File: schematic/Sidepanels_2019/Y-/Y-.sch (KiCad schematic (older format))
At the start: 53 parts, among them J1 Conn_01x04, J2 Conn_01x02

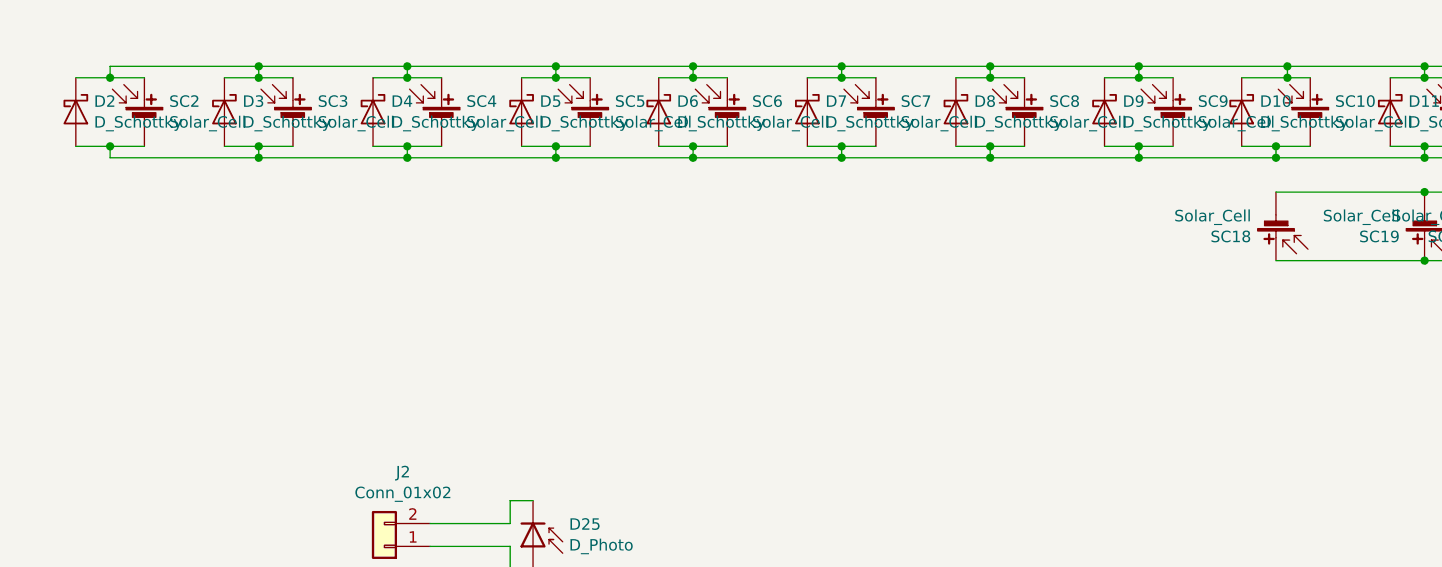
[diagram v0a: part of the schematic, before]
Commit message: Flipped and/or added TrisolX cells
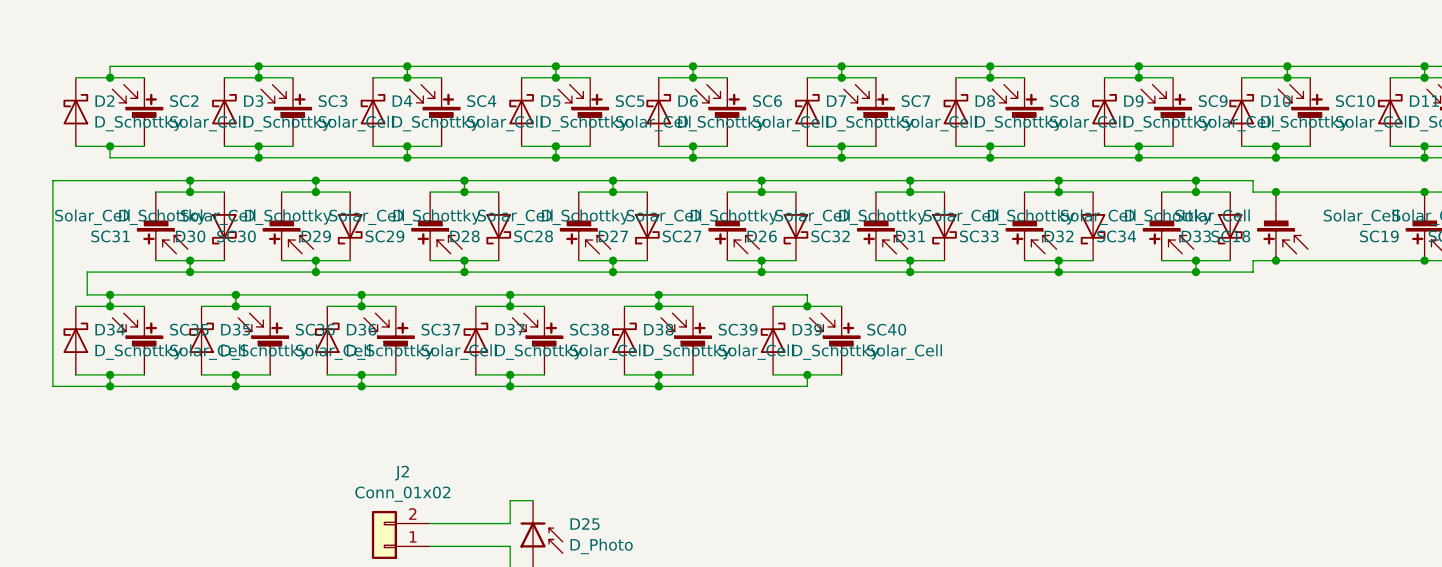
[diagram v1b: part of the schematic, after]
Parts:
- added D26, D27, D28, D29, D30, D31, D32, D33, D34, D35, D36, D37, D38, D39: D_Schottky, CySat footprints:Toshiba_CUS08F30, symbol Device:D_Schottky
- added SC27, SC28, SC29, SC30, SC31, SC32, SC33, SC34, SC35, SC36, SC37, SC38, SC39, SC40: Solar_Cell, CySat footprints:TriSelectSolarPanel_Left_Handed, symbol Device:Solar_Cell
- SC10, SC11, SC12, SC13, SC14, SC15, SC16, SC17, SC2, SC20, SC21, SC22, SC23, SC24, SC25, SC26, SC3, SC4, SC5, SC6, SC7, SC8, SC9: footprint CySat footprints:TriSelectSolarPanel -> CySat footprints:TriSelectSolarPanel_Left_Handed
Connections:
- net VCC: now also D26.1 (K), D27.1 (K), D28.1 (K), D29.1 (K), D30.1 (K), D31.1 (K), D32.1 (K), D33.1 (K), D34.1 (K), D35.1 (K), D36.1 (K), D37.1 (K), D38.1 (K), D39.1 (K), SC27.1 (+), SC28.1 (+), SC29.1 (+), SC30.1 (+), SC31.1 (+), SC32.1 (+), SC33.1 (+), SC34.1 (+), SC35.1 (+), SC36.1 (+), SC37.1 (+), SC38.1 (+), SC39.1 (+), SC40.1 (+)
- net VSS: now also D26.2 (A), D27.2 (A), D28.2 (A), D29.2 (A), D30.2 (A), D31.2 (A), D32.2 (A), D33.2 (A), D34.2 (A), D35.2 (A), D36.2 (A), D37.2 (A), D38.2 (A), D39.2 (A), SC27.2 (-), SC28.2 (-), SC29.2 (-), SC30.2 (-), SC31.2 (-), SC32.2 (-), SC33.2 (-), SC34.2 (-), SC35.2 (-), SC36.2 (-), SC37.2 (-), SC38.2 (-), SC39.2 (-), SC40.2 (-)

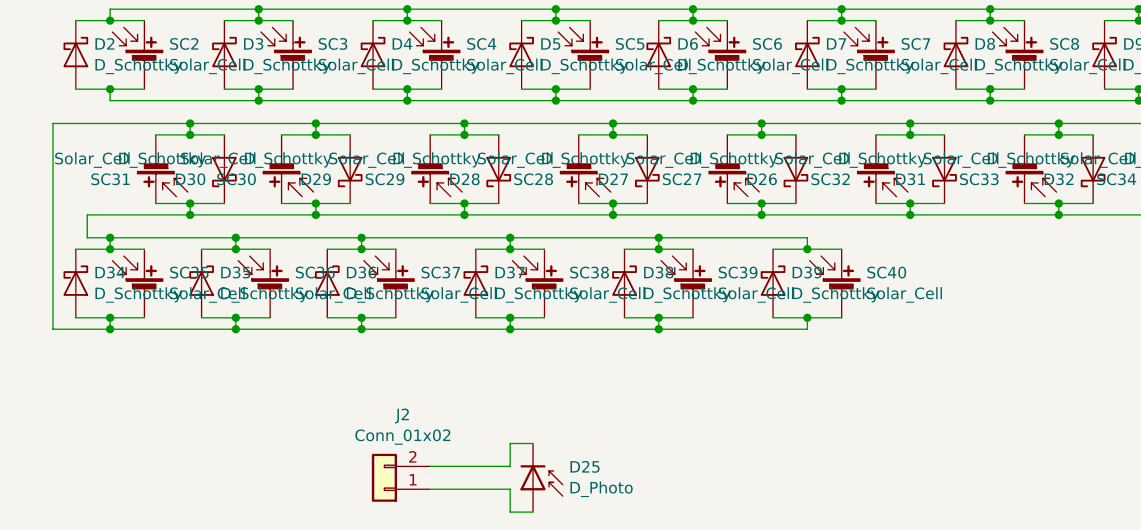
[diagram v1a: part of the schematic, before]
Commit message: Fixed TrisolX Cells
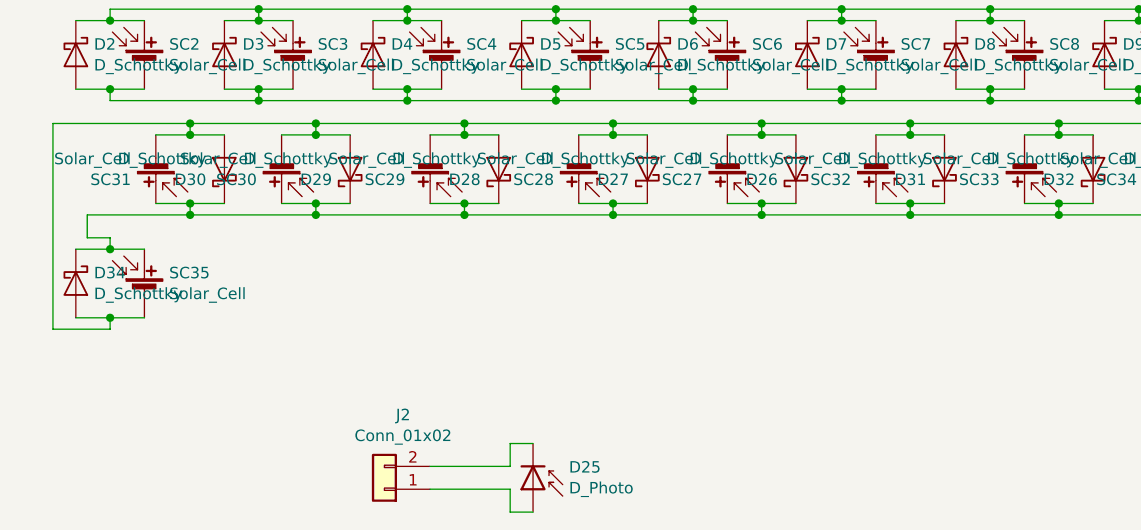
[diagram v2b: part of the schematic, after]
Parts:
- removed D35, D36, D37, D38, D39: D_Schottky, CySat footprints:Toshiba_CUS08F30, symbol Device:D_Schottky
- removed SC36, SC37, SC38, SC39, SC40: Solar_Cell, CySat footprints:TriSelectSolarPanel_Left_Handed, symbol Device:Solar_Cell
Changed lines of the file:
@@
 	5750 3700 5500 3700
 Connection ~ 5500 3700
-Wire Wire Line
-	1300 3850 1450 3850
-Wire Wire Line
-	1300 3850 1300 3800
-Wire Wire Line
-	1300 4150 1150 4150
-Wire Wire Line
-	1300 4150 1300 4200
-Connection ~ 1300 4150
-Wire Wire Line
-	1450 4150 1300 4150
-Connection ~ 1300 3850
-Wire Wire Line
-	1150 3850 1300 3850
-$Comp
-L Device:D_Schottky D35
-U 1 1 5D938735
-P 1150 4000
-F 0 "D35" V 1104 4079 50  0000 L CNN
-F 1 "D_Schottky" V 1195 4079 50  0000 L CNN
-F 2 "CySat footprints:Toshiba_CUS08F30" H 1150 4000 50  0001 C CNN
-F 3 "~" H 1150 4000 50  0001 C CNN
-	1    1150 4000
-	0    1    1    0
-$EndComp
-$Comp
-L Device:Solar_Cell SC36
-U 1 1 5D938703
-P 1450 4050
-F 0 "SC36" H 1558 4146 50  0000 L CNN
-F 1 "Solar_Cell" H 1558 4055 50  0000 L CNN
-F 2 "CySat footprints:TriSelectSolarPanel_Left_Handed" V 1450 4110 50  0001 C CNN
-F 3 "~" V 1450 4110 50  0001 C CNN
-	1    1450 4050
-	1    0    0    -1
-$EndComp
 Connection ~ 1100 3300
 Connection ~ 1100 3700
@@
 	650  3700 1100 3700
 Wire Wire Line
-	750  3800 1300 3800
-Connection ~ 750  3800
-Wire Wire Line
-	1300 4200 750  4200
-Wire Wire Line
 	500  4200 500  3300
 Wire Wire Line
@@
 Wire Wire Line
 	500  4200 750  4200
-Connection ~ 750  4200
-$Comp
-L Device:Solar_Cell SC40
-U 1 1 5DBD78C2
-P 3950 4050
-F 0 "SC40" H 4058 4146 50  0000 L CNN
-F 1 "Solar_Cell" H 4058 4055 50  0000 L CNN
-F 2 "CySat footprints:TriSelectSolarPanel_Left_Handed" V 3950 4110 50  0001 C CNN
-F 3 "~" V 3950 4110 50  0001 C CNN
-	1    3950 4050
-	1    0    0    -1
-$EndComp
-$Comp
-L Device:Solar_Cell SC39
-U 1 1 5DBD78C8
-P 3300 4050
-F 0 "SC39" H 3408 4146 50  0000 L CNN
-F 1 "Solar_Cell" H 3408 4055 50  0000 L CNN
-F 2 "CySat footprints:TriSelectSolarPanel_Left_Handed" V 3300 4110 50  0001 C CNN
-F 3 "~" V 3300 4110 50  0001 C CNN
-	1    3300 4050
-	1    0    0    -1
-$EndComp
-$Comp
-L Device:Solar_Cell SC38
-U 1 1 5DBD78CE
-P 2650 4050
-F 0 "SC38" H 2758 4146 50  0000 L CNN
-F 1 "Solar_Cell" H 2758 4055 50  0000 L CNN
-F 2 "CySat footprints:TriSelectSolarPanel_Left_Handed" V 2650 4110 50  0001 C CNN
-F 3 "~" V 2650 4110 50  0001 C CNN
-	1    2650 4050
-	1    0    0    -1
-$EndComp
-$Comp
-L Device:Solar_Cell SC37
-U 1 1 5DBD78D4
-P 2000 4050
-F 0 "SC37" H 2108 4146 50  0000 L CNN
-F 1 "Solar_Cell" H 2108 4055 50  0000 L CNN
-F 2 "CySat footprints:TriSelectSolarPanel_Left_Handed" V 2000 4110 50  0001 C CNN
-F 3 "~" V 2000 4110 50  0001 C CNN
-	1    2000 4050
-	1    0    0    -1
-$EndComp
-$Comp
-L Device:D_Schottky D36
-U 1 1 5DBD78DA
-P 1700 4000
-F 0 "D36" V 1654 4079 50  0000 L CNN
-F 1 "D_Schottky" V 1745 4079 50  0000 L CNN
-F 2 "CySat footprints:Toshiba_CUS08F30" H 1700 4000 50  0001 C CNN
-F 3 "~" H 1700 4000 50  0001 C CNN
-	1    1700 4000
-	0    1    1    0
-$EndComp
-$Comp
-L Device:D_Schottky D37
-U 1 1 5DBD78E0
-P 2350 4000
-F 0 "D37" V 2304 4079 50  0000 L CNN
-F 1 "D_Schottky" V 2395 4079 50  0000 L CNN
-F 2 "CySat footprints:Toshiba_CUS08F30" H 2350 4000 50  0001 C CNN
-F 3 "~" H 2350 4000 50  0001 C CNN
-	1    2350 4000
-	0    1    1    0
-$EndComp
-$Comp
-L Device:D_Schottky D38
-U 1 1 5DBD78E6
-P 3000 4000
-F 0 "D38" V 2954 4079 50  0000 L CNN
-F 1 "D_Schottky" V 3045 4079 50  0000 L CNN
-F 2 "CySat footprints:Toshiba_CUS08F30" H 3000 4000 50  0001 C CNN
-F 3 "~" H 3000 4000 50  0001 C CNN
-	1    3000 4000
-	0    1    1    0
-$EndComp
-$Comp
-L Device:D_Schottky D39
-U 1 1 5DBD78EC
-P 3650 4000
-F 0 "D39" V 3604 4079 50  0000 L CNN
-F 1 "D_Schottky" V 3695 4079 50  0000 L CNN
-F 2 "CySat footprints:Toshiba_CUS08F30" H 3650 4000 50  0001 C CNN
-F 3 "~" H 3650 4000 50  0001 C CNN
-	1    3650 4000
-	0    1    1    0
-$EndComp
-Wire Wire Line
-	1700 3850 1850 3850
-Wire Wire Line
-	2000 4150 1850 4150
-Wire Wire Line
-	2350 3850 2500 3850
-Wire Wire Line
-	2650 4150 2500 4150
-Wire Wire Line
-	3000 3850 3150 3850
-Wire Wire Line
-	3300 4150 3150 4150
-Wire Wire Line
-	3650 3850 3800 3850
-Wire Wire Line
-	3950 4150 3800 4150
-Wire Wire Line
-	1850 3800 2500 3800
-Wire Wire Line
-	1850 3800 1850 3850
-Connection ~ 1850 3850
-Wire Wire Line
-	1850 3850 2000 3850
-Wire Wire Line
-	1850 4150 1850 4200
-Wire Wire Line
-	1850 4200 2500 4200
-Connection ~ 1850 4150
-Wire Wire Line
-	1850 4150 1700 4150
-Wire Wire Line
-	2500 4150 2500 4200
-Connection ~ 2500 4150
-Wire Wire Line
-	2500 4150 2350 4150
-Connection ~ 2500 4200
-Wire Wire Line
-	2500 4200 3150 4200
-Wire Wire Line
-	3150 4150 3150 4200
-Connection ~ 3150 4150
-Wire Wire Line
-	3150 4150 3000 4150
-Connection ~ 3150 4200
-Wire Wire Line
-	3150 4200 3800 4200
-Wire Wire Line
-	2500 3850 2500 3800
-Connection ~ 2500 3850
-Wire Wire Line
-	2500 3850 2650 3850
-Connection ~ 2500 3800
-Wire Wire Line
-	2500 3800 3150 3800
-Wire Wire Line
-	3150 3850 3150 3800
-Connection ~ 3150 3850
-Wire Wire Line
-	3150 3850 3300 3850
-Connection ~ 3150 3800
-Wire Wire Line
-	3150 3800 3800 3800
-Wire Wire Line
-	3800 3850 3800 3800
-Connection ~ 3800 3850
-Wire Wire Line
-	3800 3850 3950 3850
-Wire Wire Line
-	3800 4150 3800 4200
-Connection ~ 3800 4150
-Wire Wire Line
-	3800 4150 3650 4150
-Wire Wire Line
-	1300 3800 1850 3800
-Connection ~ 1300 3800
-Connection ~ 1850 3800
-Wire Wire Line
-	1850 4200 1300 4200
-Connection ~ 1850 4200
-Connection ~ 1300 4200
 $EndSCHEMATC

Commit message: Updates
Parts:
- removed D1, D10, D11, D12, D13, D14, D15, D16, D17, D18, D19, D2, D20, D21, D22, D23, D24, D26, D27, D28, D29, D3, D30, D31, D32, D33, D34, D4, D5, D6, D7, D8, D9: D_Schottky, CySat footprints:Toshiba_CUS08F30, symbol Device:D_Schottky
- removed SC1: Solar_Cell, CySat footprints:ISS_SolarCell, symbol Device:Solar_Cell
- removed SC10, SC11, SC12, SC13, SC14, SC15, SC16, SC17, SC2, SC20, SC21, SC22, SC23, SC24, SC25, SC26, SC27, SC28, SC29, SC30, SC31, SC32, SC33, SC34, SC35, SC7, SC8, SC9: Solar_Cell, CySat footprints:TriSelectSolarPanel_Left_Handed, symbol Device:Solar_Cell
- D1: renamed from D25; footprint CySat footprints:Sun_Sensor -> Diode_SMD:D_0805_2012Metric
- SC1: renamed from SC18; footprint CySat footprints:Spectrolab -> CySat_Solar:Spectrolab
- SC2: renamed from SC19; footprint CySat footprints:Spectrolab -> CySat_Solar:Spectrolab
- SC3, SC4, SC5, SC6: footprint CySat footprints:TriSelectSolarPanel_Left_Handed -> CySat_Solar:Spectrolab
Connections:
- net VCC: no longer SC1.1 (+), SC2.1 (+), SC3.1 (+), SC4.1 (+), SC5.1 (+), SC6.1 (+)
- net VSS: no longer SC1.2 (-), SC2.2 (-), SC3.2 (-), SC4.2 (-), SC5.2 (-), SC6.2 (-)
- new net: SC1.1 (+), SC2.1 (+), SC3.1 (+), SC4.1 (+), SC5.1 (+), SC6.1 (+)
- new net: SC1.2 (-), SC2.2 (-), SC3.2 (-), SC4.2 (-), SC5.2 (-), SC6.2 (-)
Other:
- moved on the sheet: SC1, SC2

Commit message: Completed y-
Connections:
- net VCC: now also SC1.1 (+), SC2.1 (+), SC3.1 (+), SC4.1 (+), SC5.1 (+), SC6.1 (+)
- net VSS: now also SC1.2 (-), SC2.2 (-), SC3.2 (-), SC4.2 (-), SC5.2 (-), SC6.2 (-)
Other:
- moved on the sheet: SC1, SC2, SC3, SC4, SC5, SC6
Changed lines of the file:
@@
 L Device:Solar_Cell SC1
 U 1 1 5CAFDDDE
-P 2000 3350
-F 0 "SC1" H 2108 3446 50  0000 L CNN
-F 1 "Solar_Cell" H 2108 3355 50  0000 L CNN
-F 2 "CySat_Solar:Spectrolab" V 2000 3410 50  0001 C CNN
-F 3 "~" V 2000 3410 50  0001 C CNN
-	1    2000 3350
-	-1   0    0    1
+P 2000 3450
+F 0 "SC1" H 2108 3546 50  0000 L CNN
+F 1 "Solar_Cell" H 2108 3455 50  0000 L CNN
+F 2 "CySat_Solar:Spectrolab" V 2000 3510 50  0001 C CNN
+F 3 "~" V 2000 3510 50  0001 C CNN
+	1    2000 3450
+	1    0    0    -1
 $EndComp
 $Comp
 L Device:Solar_Cell SC2
 U 1 1 5CAFE43B
-P 2650 3350
-F 0 "SC2" H 2758 3446 50  0000 L CNN
-F 1 "Solar_Cell" H 2758 3355 50  0000 L CNN
-F 2 "CySat_Solar:Spectrolab" V 2650 3410 50  0001 C CNN
-F 3 "~" V 2650 3410 50  0001 C CNN
-	1    2650 3350
-	-1   0    0    1
+P 2550 3450
+F 0 "SC2" H 2658 3546 50  0000 L CNN
+F 1 "Solar_Cell" H 2658 3455 50  0000 L CNN
+F 2 "CySat_Solar:Spectrolab" V 2550 3510 50  0001 C CNN
+F 3 "~" V 2550 3510 50  0001 C CNN
+	1    2550 3450
+	1    0    0    -1
 $EndComp
-Wire Wire Line
-	2000 3250 2650 3250
-Wire Wire Line
-	2000 3550 2650 3550
 $Comp
 L Device:Solar_Cell SC3
 U 1 1 5F2390EB
-P 3100 3350
-F 0 "SC3" H 3208 3446 50  0000 L CNN
-F 1 "Solar_Cell" H 3208 3355 50  0000 L CNN
-F 2 "CySat_Solar:Spectrolab" V 3100 3410 50  0001 C CNN
-F 3 "~" V 3100 3410 50  0001 C CNN
-	1    3100 3350
-	-1   0    0    1
+P 3100 3450
+F 0 "SC3" H 3208 3546 50  0000 L CNN
+F 1 "Solar_Cell" H 3208 3455 50  0000 L CNN
+F 2 "CySat_Solar:Spectrolab" V 3100 3510 50  0001 C CNN
+F 3 "~" V 3100 3510 50  0001 C CNN
+	1    3100 3450
+	1    0    0    -1
 $EndComp
 $Comp
 L Device:Solar_Cell SC4
 U 1 1 5F23F079
-P 3600 3350
-F 0 "SC4" H 3708 3446 50  0000 L CNN
-F 1 "Solar_Cell" H 3708 3355 50  0000 L CNN
-F 2 "CySat_Solar:Spectrolab" V 3600 3410 50  0001 C CNN
-F 3 "~" V 3600 3410 50  0001 C CNN
-	1    3600 3350
-	-1   0    0    1
+P 3600 3450
+F 0 "SC4" H 3708 3546 50  0000 L CNN
+F 1 "Solar_Cell" H 3708 3455 50  0000 L CNN
+F 2 "CySat_Solar:Spectrolab" V 3600 3510 50  0001 C CNN
+F 3 "~" V 3600 3510 50  0001 C CNN
+	1    3600 3450
+	1    0    0    -1
 $EndComp
 $Comp
 L Device:Solar_Cell SC5
 U 1 1 5F23F083
-P 4250 3350
-F 0 "SC5" H 4358 3446 50  0000 L CNN
-F 1 "Solar_Cell" H 4358 3355 50  0000 L CNN
-F 2 "CySat_Solar:Spectrolab" V 4250 3410 50  0001 C CNN
-F 3 "~" V 4250 3410 50  0001 C CNN
-	1    4250 3350
-	-1   0    0    1
+P 4150 3450
+F 0 "SC5" H 4258 3546 50  0000 L CNN
+F 1 "Solar_Cell" H 4258 3455 50  0000 L CNN
+F 2 "CySat_Solar:Spectrolab" V 4150 3510 50  0001 C CNN
+F 3 "~" V 4150 3510 50  0001 C CNN
+	1    4150 3450
+	1    0    0    -1
 $EndComp
-Wire Wire Line
-	3600 3250 4250 3250
-Wire Wire Line
-	3600 3550 4250 3550
 $Comp
 L Device:Solar_Cell SC6
 U 1 1 5F23F08F
-P 4700 3350
-F 0 "SC6" H 4808 3446 50  0000 L CNN
-F 1 "Solar_Cell" H 4808 3355 50  0000 L CNN
-F 2 "CySat_Solar:Spectrolab" V 4700 3410 50  0001 C CNN
-F 3 "~" V 4700 3410 50  0001 C CNN
-	1    4700 3350
+P 4700 3450
+F 0 "SC6" H 4808 3546 50  0000 L CNN
+F 1 "Solar_Cell" H 4808 3455 50  0000 L CNN
+F 2 "CySat_Solar:Spectrolab" V 4700 3510 50  0001 C CNN
+F 3 "~" V 4700 3510 50  0001 C CNN
+	1    4700 3450
+	1    0    0    -1
+$EndComp
+$Comp
+L power:VSS #PWR0101
+U 1 1 5F17F317
+P 3350 3550
+F 0 "#PWR0101" H 3350 3400 50  0001 C CNN
+F 1 "VSS" H 3365 3723 50  0000 C CNN
+F 2 "" H 3350 3550 50  0001 C CNN
+F 3 "" H 3350 3550 50  0001 C CNN
+	1    3350 3550
 	-1   0    0    1
 $EndComp
+Connection ~ 3350 3550
+$Comp
+L power:VCC #PWR0102
+U 1 1 5F18055D
+P 3350 3250
+F 0 "#PWR0102" H 3350 3100 50  0001 C CNN
+F 1 "VCC" H 3365 3423 50  0000 C CNN
+F 2 "" H 3350 3250 50  0001 C CNN
+F 3 "" H 3350 3250 50  0001 C CNN
+	1    3350 3250
+	1    0    0    -1
+$EndComp
+Connection ~ 3350 3250
 Wire Wire Line
-	2650 3250 3100 3250
-Connection ~ 2650 3250
+	2000 3250 2550 3250
 Wire Wire Line
-	3100 3250 3600 3250
+	2000 3550 2550 3550
 Connection ~ 3100 3250
+Wire Wire Line
+	3100 3250 3350 3250
+Connection ~ 3100 3550
+Wire Wire Line
+	3100 3550 3350 3550
+Wire Wire Line
+	3350 3250 3600 3250
+Wire Wire Line
+	3350 3550 3600 3550
 Connection ~ 3600 3250
-Wire Wire Line
-	4250 3250 4700 3250
-Connection ~ 4250 3250
-Wire Wire Line
-	2650 3550 3100 3550
-Connection ~ 2650 3550
-Wire Wire Line
-	3100 3550 3600 3550
-Connection ~ 3100 3550
 Connection ~ 3600 3550
 Wire Wire Line
-	4250 3550 4700 3550
-Connection ~ 4250 3550
+	3600 3250 4150 3250
+Wire Wire Line
+	3600 3550 4150 3550
+Connection ~ 4150 3250
+Connection ~ 4150 3550
+Wire Wire Line
+	4150 3250 4700 3250
+Wire Wire Line
+	4150 3550 4700 3550
+Connection ~ 2550 3250
+Connection ~ 2550 3550
+Wire Wire Line
+	2550 3250 3100 3250
+Wire Wire Line
+	2550 3550 3100 3550
 $EndSCHEMATC
